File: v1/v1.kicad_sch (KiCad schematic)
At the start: 66 parts, among them CON1 SNES-CONN

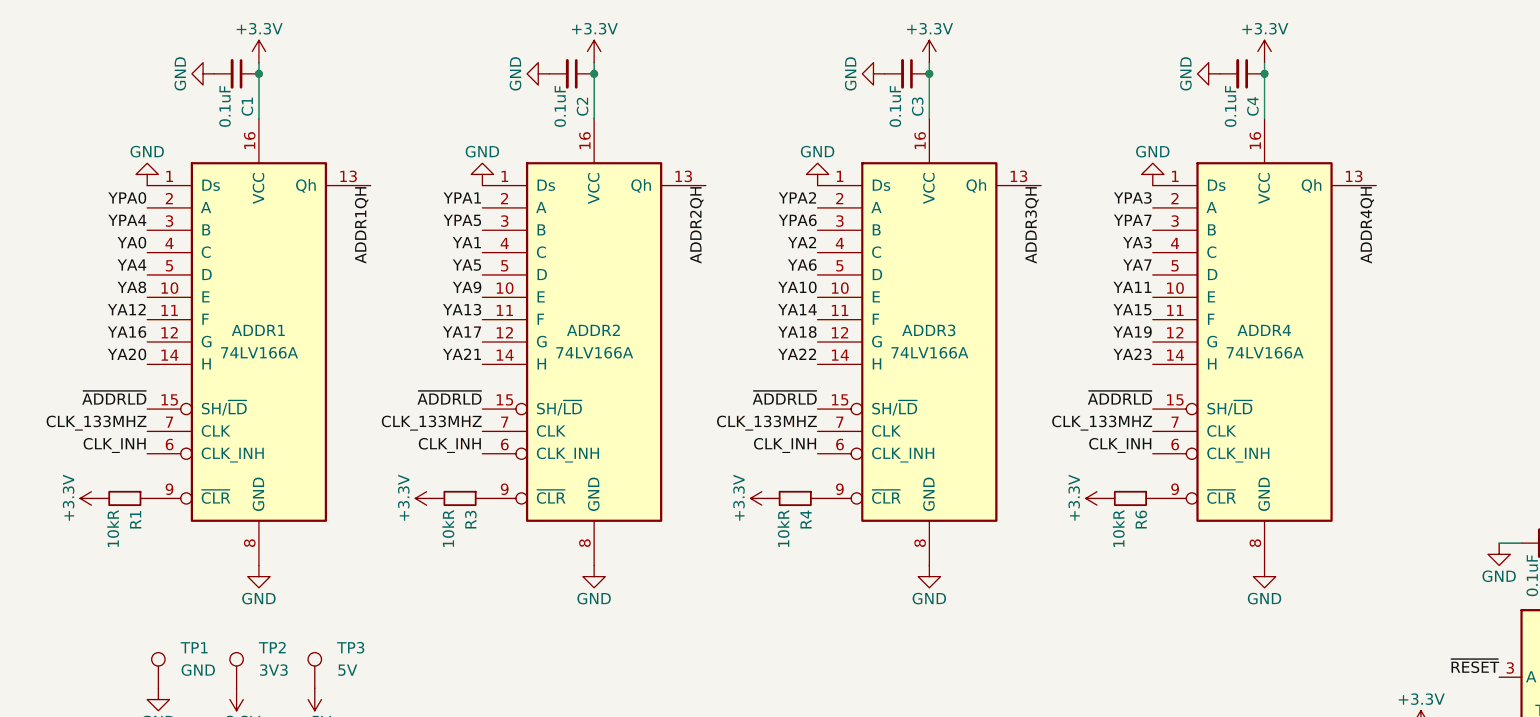
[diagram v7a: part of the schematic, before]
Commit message: v1: restarting routing of shift registers in new orientation with replacement components
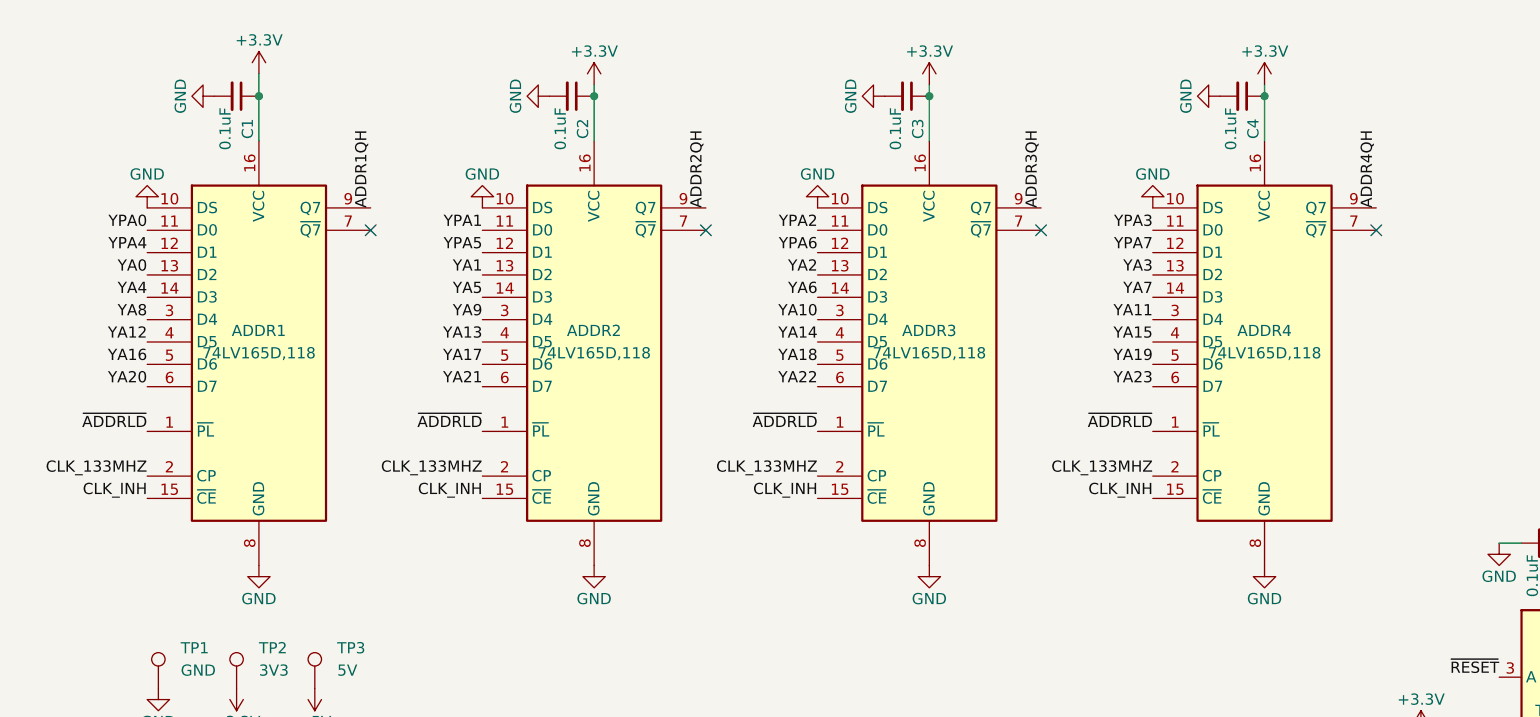
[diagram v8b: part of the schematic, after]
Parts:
- removed R1, R3, R4, R6: 10kR, Resistor_SMD:R_1206_3216Metric_Pad1.30x1.75mm_HandSolder, symbol Device:R_Small
- ADDR1, ADDR2, ADDR3, ADDR4: value 74LV166A -> 74LV165D,118; symbol 74xx:74LV166A -> 74xx:74HC165; LCSC C2860649 -> C547919
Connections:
- net ADDR1QH: now also ADDR1.9 (Q7); no longer ADDR1.13 (Qh)
- net ADDR2QH: now also ADDR2.9 (Q7); no longer ADDR2.13 (Qh)
- net ADDR3QH: now also ADDR3.9 (Q7); no longer ADDR3.13 (Qh)
- net ADDR4QH: now also ADDR4.9 (Q7); no longer ADDR4.13 (Qh)
- net CLK_133MHZ: now also ADDR1.2 (CP), ADDR2.2 (CP), ADDR3.2 (CP), ADDR4.2 (CP); no longer ADDR1.7 (CLK), ADDR2.7 (CLK), ADDR3.7 (CLK), ADDR4.7 (CLK)
- net CLK_INH: now also ADDR1.15 (~{CE}), ADDR2.15 (~{CE}), ADDR3.15 (~{CE}), ADDR4.15 (~{CE}); no longer ADDR1.6 (CLK_INH), ADDR2.6 (CLK_INH), ADDR3.6 (CLK_INH), ADDR4.6 (CLK_INH)
- net GND: now also ADDR1.10 (DS), ADDR2.10 (DS), ADDR3.10 (DS), ADDR4.10 (DS); no longer ADDR1.1 (Ds), ADDR2.1 (Ds), ADDR3.1 (Ds), ADDR4.1 (Ds)
- net YA0: now also ADDR1.13 (D2); no longer ADDR1.4 (C)
- net YA1: now also ADDR2.13 (D2); no longer ADDR2.4 (C)
- net YA10: now also ADDR3.3 (D4); no longer ADDR3.10 (E)
- net YA11: now also ADDR4.3 (D4); no longer ADDR4.10 (E)
- net YA12: now also ADDR1.4 (D5); no longer ADDR1.11 (F)
- net YA13: now also ADDR2.4 (D5); no longer ADDR2.11 (F)
- net YA14: now also ADDR3.4 (D5); no longer ADDR3.11 (F)
- net YA15: now also ADDR4.4 (D5); no longer ADDR4.11 (F)
- net YA16: now also ADDR1.5 (D6); no longer ADDR1.12 (G)
- net YA17: now also ADDR2.5 (D6); no longer ADDR2.12 (G)
- net YA18: now also ADDR3.5 (D6); no longer ADDR3.12 (G)
- net YA19: now also ADDR4.5 (D6); no longer ADDR4.12 (G)
- net YA2: now also ADDR3.13 (D2); no longer ADDR3.4 (C)
- net YA20: now also ADDR1.6 (D7); no longer ADDR1.14 (H)
- net YA21: now also ADDR2.6 (D7); no longer ADDR2.14 (H)
- net YA22: now also ADDR3.6 (D7); no longer ADDR3.14 (H)
- net YA23: now also ADDR4.6 (D7); no longer ADDR4.14 (H)
- net YA3: now also ADDR4.13 (D2); no longer ADDR4.4 (C)
- net YA4: now also ADDR1.14 (D3); no longer ADDR1.5 (D)
- net YA5: now also ADDR2.14 (D3); no longer ADDR2.5 (D)
- net YA6: now also ADDR3.14 (D3); no longer ADDR3.5 (D)
- net YA7: now also ADDR4.14 (D3); no longer ADDR4.5 (D)
- net YA8: now also ADDR1.3 (D4); no longer ADDR1.10 (E)
- net YA9: now also ADDR2.3 (D4); no longer ADDR2.10 (E)
- net YPA0: now also ADDR1.11 (D0); no longer ADDR1.2 (A)
- net YPA1: now also ADDR2.11 (D0); no longer ADDR2.2 (A)
- net YPA2: now also ADDR3.11 (D0); no longer ADDR3.2 (A)
- net YPA3: now also ADDR4.11 (D0); no longer ADDR4.2 (A)
- net YPA4: now also ADDR1.12 (D1); no longer ADDR1.3 (B)
- net YPA5: now also ADDR2.12 (D1); no longer ADDR2.3 (B)
- net YPA6: now also ADDR3.12 (D1); no longer ADDR3.3 (B)
- net YPA7: now also ADDR4.12 (D1); no longer ADDR4.3 (B)
- net ~{ADDRLD}: now also ADDR1.1 (~{PL}), ADDR2.1 (~{PL}), ADDR3.1 (~{PL}), ADDR4.1 (~{PL}); no longer ADDR1.15 (SH/~{LD}), ADDR2.15 (SH/~{LD}), ADDR3.15 (SH/~{LD}), ADDR4.15 (SH/~{LD})
- no-connect marks 8 -> 12
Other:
- moved on the sheet: C1, C2, C3, C4
